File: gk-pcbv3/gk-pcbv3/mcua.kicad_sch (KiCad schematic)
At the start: 12 parts, among them J12 Conn_01x03, SW1 SW_Push, U4 STM32H7S7L8H6H, Y2 32.768kHz R26-32.768-12.5

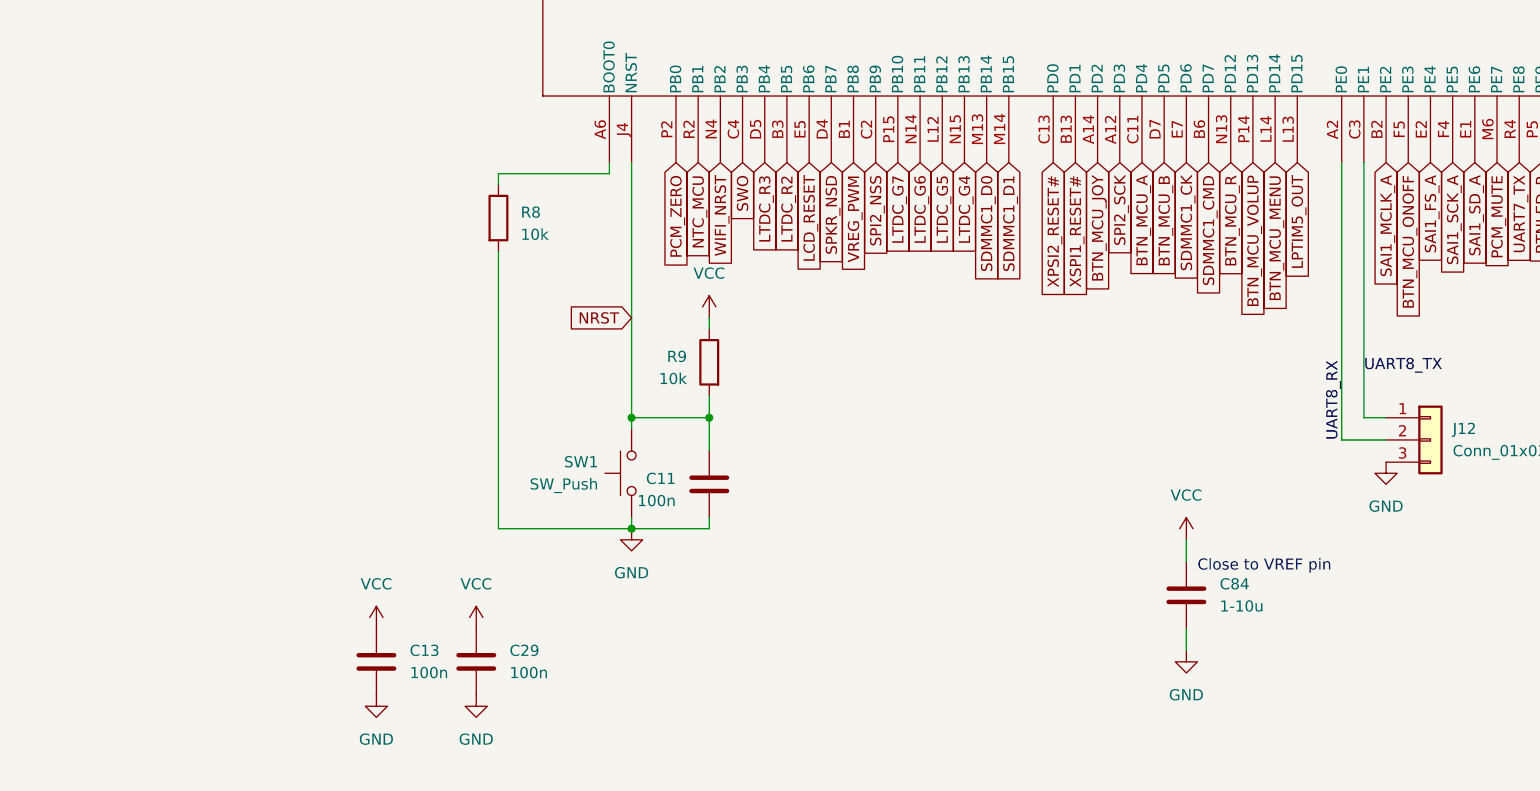
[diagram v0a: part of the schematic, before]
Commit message: redesign for better signal integrity
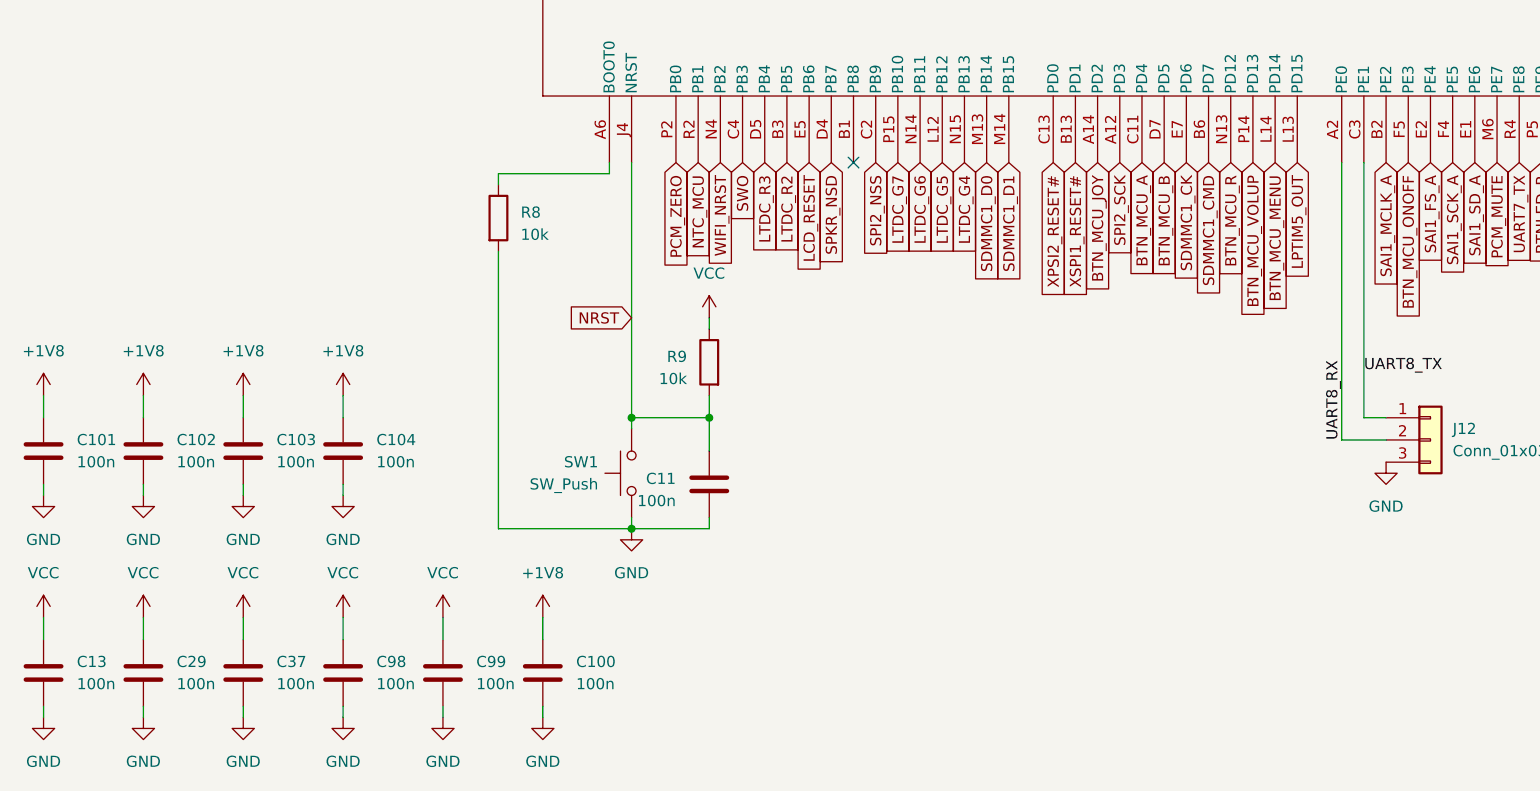
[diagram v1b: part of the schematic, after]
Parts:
- removed C84: 1-10u, Capacitor_SMD:C_0805_2012Metric, symbol Device:C
- added C100, C101, C102, C103, C104, C37, C98, C99: 100n, Capacitor_SMD:C_0402_1005Metric, symbol Device:C
- C13, C29: footprint Capacitor_SMD:C_0603_1608Metric -> Capacitor_SMD:C_0402_1005Metric
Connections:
- net GND: now also C100.2, C101.2, C102.2, C103.2, C104.2, C37.2, C98.2, C99.2
- net VCC: now also C37.1, C98.1, C99.1
- net VREG_PWM: no longer names the net of U4.B1 (PB8)
- new net +1V8: C100.1, C101.1, C102.1, C103.1, C104.1
- no-connect marks 3 -> 4
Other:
- note removed: "Close to VREF pin"

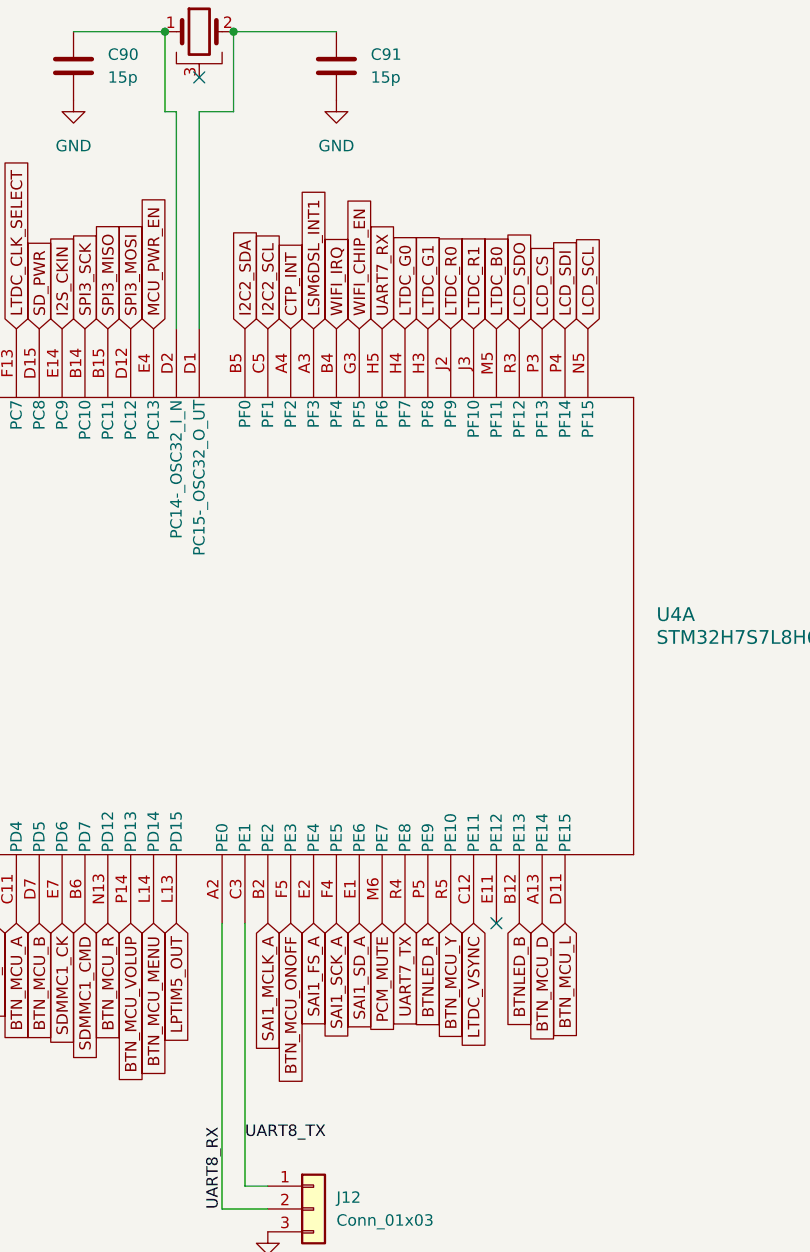
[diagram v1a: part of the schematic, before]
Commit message: Route top end of board Remove vbat stat LED
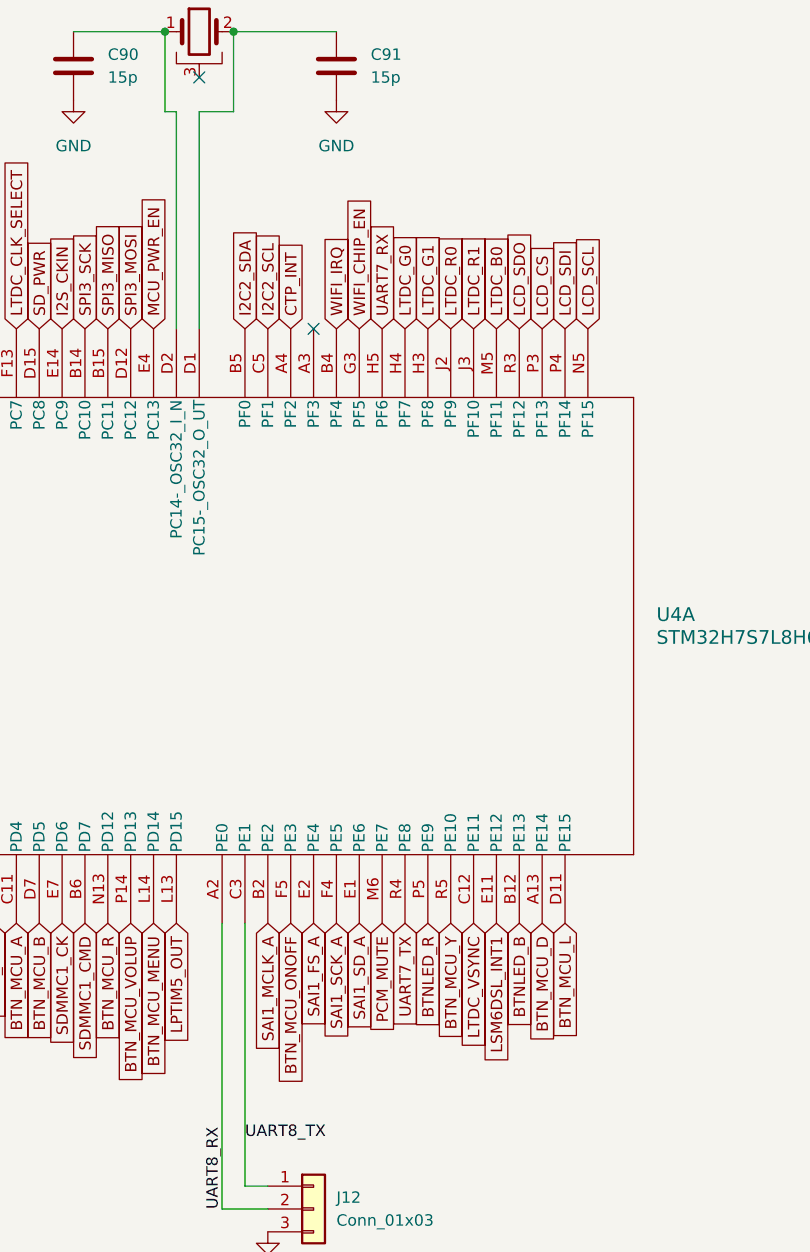
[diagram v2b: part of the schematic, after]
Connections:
- net LSM6DSL_INT1: now also U4.E11 (PE12); no longer U4.A3 (PF3)
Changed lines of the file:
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@@
 	)
 	(no_connect
-		(at 199.39 125.73)
+		(at 179.07 59.69)
 	)
 	(no_connect
@@
 	(global_label "LSM6DSL_INT1"
 		(shape input)
-		(at 179.07 59.69 90)
-		(fields_autoplaced yes)
-		(effects
-			(font
-				(size 1.27 1.27)
-			)
-			(justify left)
-		)
-		(property "Intersheetrefs" "${INTERSHEET_REFS}"
-			(at 179.07 43.2187 90)
-			(effects
-				(font
-					(size 1.27 1.27)
-				)
-				(justify left)
-				(hide yes)
-			)
+		(at 199.39 125.73 270)
+		(fields_autoplaced yes)
+		(effects
+			(font
+				(size 1.27 1.27)
+			)
+			(justify right)
+		)
+		(property "Intersheetrefs" "${INTERSHEET_REFS}"
+			(at 199.39 142.2013 90)
+			(effects
+				(font
+					(size 1.27 1.27)
+				)
+				(justify right)
+				(hide yes)
+			)

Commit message: gerbers for v3.1
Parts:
- added TP16: TestPoint, Connector_PinHeader_2.54mm:PinHeader_1x01_P2.54mm_Vertical, symbol Connector:TestPoint
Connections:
- net CTP_NRESET: now also U4.A3 (PF3); no longer U4.K3 (PC0)
- new net: TP16.1, U4.K3 (PC0)
- no-connect marks 4 -> 3

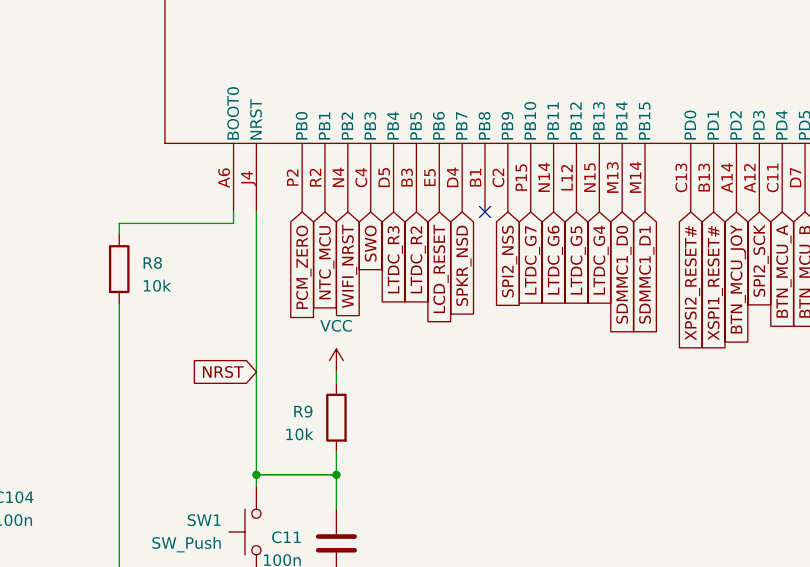
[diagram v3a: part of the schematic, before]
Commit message: update schematics for new vreg design
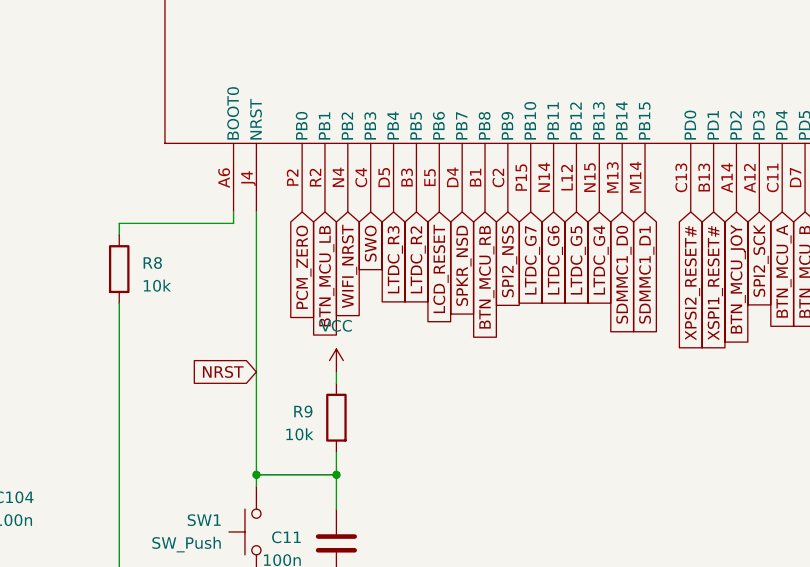
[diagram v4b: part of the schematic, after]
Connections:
- net BTN_MCU_RB: now reaches U4.B1 (PB8)
- net NTC_MCU renamed BTN_MCU_LB
- no-connect marks 3 -> 2
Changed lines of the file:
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@@
-	)
-	(no_connect
-		(at 113.03 125.73)
 	)
 	(no_connect
@@
 		)
 	)
+	(global_label "BTN_MCU_LB"
+		(shape input)
+		(at 95.25 125.73 270)
+		(fields_autoplaced yes)
+		(effects
+			(font
+				(size 1.27 1.27)
+			)
+			(justify right)
+		)
+		(property "Intersheetrefs" "${INTERSHEET_REFS}"
+			(at 95.25 140.5685 90)
+			(effects
+				(font
+					(size 1.27 1.27)
+				)
+				(justify right)
+				(hide yes)
+			)
+		)
+	)
 	(global_label "I2C2_SCL"
 		(shape input)
@@
 		)
 	)
+	(global_label "BTN_MCU_RB"
+		(shape input)
+		(at 113.03 125.73 270)
+		(fields_autoplaced yes)
+		(effects
+			(font
+				(size 1.27 1.27)
+			)
+			(justify right)
+		)
+		(property "Intersheetrefs" "${INTERSHEET_REFS}"
+			(at 113.03 140.8104 90)
+			(effects
+				(font
+					(size 1.27 1.27)
+				)
+				(justify right)
+				(hide yes)
+			)
+		)
+	)
 	(global_label "UART7_RX"
 		(shape input)
@@
 				(hide yes)
 			)
-		)
-	)
-	(global_label "NTC_MCU"
-		(shape input)
-		(at 95.25 125.73 270)
-		(fields_autoplaced yes)
-		(effects
-			(font
-				(size 1.27 1.27)
-			)
-			(justify right)
-		)
-		(property "Intersheetrefs" "${INTERSHEET_REFS}"
-			(at 95.25 137.3028 90)
-			(effects
-				(font
-					(size 1.27 1.27)
-				)
-				(justify right)
-				(hide yes)
-			)

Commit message: new gerbers
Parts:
- removed TP16: TestPoint, Connector_PinHeader_2.54mm:PinHeader_1x01_P2.54mm_Vertical, symbol Connector:TestPoint
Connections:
- net BAT_SYSOFF: now reaches U4.K3 (PC0)
- net LSM6DSL_INT1 renamed BOOST_EN
